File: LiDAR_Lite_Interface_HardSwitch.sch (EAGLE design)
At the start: 30 parts, among them J1 CONN_6SCREW_2.54, J2 CONN_42.54_SCREW, Q1 2N7002, Q2 2N7002, Q3 DMG3404, Q4 MOSFET_PCH-NX2301P, U1 TLV61220DBV, U2 TS5A23157DGS

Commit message: Updated layout, added variants
Improved layout, potentially add button, then ready to send to fab. Added variations of layout for potential future alteration
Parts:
- removed U2: TS5A23157DGS, bschulz:TS5A23157DGS
- added S1: SWITCH_DPDTJS_GULLWING, bschulz:SWITCH_DPDTJS_GULLWING
- C1: DIGIKEY (none) -> 493-2182-1-ND; MF (none) -> Nichicon; MPN (none) -> UWT1C681MNL1GS
- D1: DIGIKEY (none) -> 732-4978-1-ND; MF (none) -> Wurth; MPN (none) -> 150060RS75000
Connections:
- removed net OUTPUT_CTRL: U2.IN1, U2.IN2, U3.PA6
- net 5V: no longer U2.VCC
- net GND: no longer U2.GND
- net POWER_SW: now also U3.PA6; no longer U3.PA5
- net RX: now also S1.O2; no longer U2.NO2
- net SCL: now also S1.S2; no longer U2.NC1
- net SDA: now also S1.S1; no longer U2.NC2
- net SIG1: now also S1.P1; no longer U2.COM1
- net SIG2: now also S1.P2; no longer U2.COM2
- net TX: now also S1.O1; no longer U2.NO1
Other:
- note added: "RED"
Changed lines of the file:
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@@
 <part name="R1" library="bschulz_passives" deviceset="R-EU_" device="R0603" technology="4.7K" value="4.7k"/>
 <part name="R2" library="bschulz_passives" deviceset="R-EU_" device="R0603" technology="4.7K" value="4.7k"/>
-<part name="C1" library="bschulz_passives" deviceset="CPOL-EU" device="UW-10X10"/>
+<part name="C1" library="bschulz_passives" deviceset="CPOL-EU" device="UW-10X10">
+<spice>
+<pinmapping spiceprefix="C">
+<pinmap gate="G$1" pin="+" pinorder="1"/>
+<pinmap gate="G$1" pin="-" pinorder="2"/>
+</pinmapping>
+</spice>
+<attribute name="DIGIKEY" value="493-2182-1-ND"/>
+<attribute name="MF" value="Nichicon"/>
+<attribute name="MPN" value="UWT1C681MNL1GS"/>
+</part>
 <part name="GND1" library="supply1" library_urn="urn:adsk.eagle:library:371" deviceset="GND" device=""/>
 <part name="Q1" library="bschulz" deviceset="MOSFET-NCH" device="-2N7002P" value="2N7002"/>
@@
 <part name="R9" library="bschulz_passives" deviceset="R-EU_" device="R0603" technology="10K" value="10k"/>
 <part name="GND6" library="supply1" library_urn="urn:adsk.eagle:library:371" deviceset="GND" device=""/>
-<part name="D1" library="bschulz" deviceset="LED" device="0603" value="LED0603"/>
+<part name="D1" library="bschulz" deviceset="LED" device="0603" value="LED0603">
+<attribute name="DIGIKEY" value="732-4978-1-ND"/>
+<attribute name="MF" value="Wurth"/>
+<attribute name="MPN" value="150060RS75000"/>
+</part>
 <part name="R10" library="bschulz_passives" deviceset="R-EU_" device="R0603" technology="330"/>
 <part name="GND20" library="supply1" library_urn="urn:adsk.eagle:library:371" deviceset="GND" device=""/>
 <part name="R11" library="bschulz_passives" deviceset="R-EU_" device="R0603" technology="1K" value="1k"/>
-<part name="U2" library="bschulz" deviceset="TS5A23157" device="DGS"/>
+<part name="S1" library="bschulz" deviceset="SWITCH_DPDT" device="JS_GULLWING"/>
 </parts>
 <sheets>
@@
 <plain>
 <text x="-22.86" y="7.62" size="1.778" layer="91">Software I2C!</text>
+<text x="5.08" y="71.12" size="1.778" layer="91" rot="R90">RED</text>
 </plain>
 <instances>
@@
 <attribute name="NAME" x="26.543" y="38.5826" size="1.778" layer="95"/>
 <attribute name="VALUE" x="26.543" y="33.5026" size="1.778" layer="96"/>
+<attribute name="MPN" x="25.4" y="38.1" size="1.778" layer="96" display="off"/>
+<attribute name="MF" x="25.4" y="38.1" size="1.778" layer="96" display="off"/>
+<attribute name="DIGIKEY" x="25.4" y="38.1" size="1.778" layer="96" display="off"/>
 </instance>
 <instance part="GND1" gate="1" x="25.4" y="27.94" smashed="yes">
@@
 <attribute name="VALUE" x="113.03" y="95.758" size="1.778" layer="96"/>
 </instance>
-<instance part="U2" gate="G$1" x="152.4" y="81.28" smashed="yes">
-<attribute name="DISP" x="152.4" y="95.758" size="1.778" layer="95" ratio="15" align="center"/>
-<attribute name="NAME" x="152.4" y="64.008" size="1.778" layer="95" ratio="15" align="center"/>
+<instance part="S1" gate="G$1" x="147.32" y="76.2" smashed="yes" rot="R180">
+<attribute name="VALUE" x="148.59" y="82.55" size="1.778" layer="96" font="vector" rot="R180" align="top-center"/>
+<attribute name="NAME" x="148.59" y="67.818" size="1.778" layer="95" font="vector" rot="R180" align="bottom-center"/>
 </instance>
 </instances>
@@
 <wire x1="10.16" y1="68.58" x2="10.16" y2="66.04" width="0.1524" layer="91"/>
 <pinref part="GND20" gate="1" pin="GND"/>
-</segment>
-<segment>
-<pinref part="U2" gate="G$1" pin="GND"/>
-<wire x1="139.7" y1="88.9" x2="134.62" y2="88.9" width="0.1524" layer="91"/>
-<label x="134.62" y="88.9" size="1.778" layer="95" rot="R180" xref="yes"/>
 </segment>
 <segment>
@@
 </segment>
 <segment>
-<pinref part="U2" gate="G$1" pin="NC2"/>
-<wire x1="139.7" y1="71.12" x2="134.62" y2="71.12" width="0.1524" layer="91"/>
-<label x="134.62" y="71.12" size="1.778" layer="95" rot="R180" xref="yes"/>
+<wire x1="144.78" y1="73.66" x2="139.7" y2="73.66" width="0.1524" layer="91"/>
+<label x="139.7" y="73.66" size="1.778" layer="95" rot="R180" xref="yes"/>
+<pinref part="S1" gate="G$1" pin="S1"/>
 </segment>
 </net>
@@
 </segment>
 <segment>
-<pinref part="U2" gate="G$1" pin="NC1"/>
-<wire x1="139.7" y1="81.28" x2="134.62" y2="81.28" width="0.1524" layer="91"/>
-<label x="134.62" y="81.28" size="1.778" layer="95" rot="R180" xref="yes"/>
+<wire x1="144.78" y1="81.28" x2="139.7" y2="81.28" width="0.1524" layer="91"/>
+<label x="139.7" y="81.28" size="1.778" layer="95" rot="R180" xref="yes"/>
+<pinref part="S1" gate="G$1" pin="S2"/>
 </segment>
 </net>
@@
 </segment>
 <segment>
-<pinref part="U2" gate="G$1" pin="COM2"/>
-<wire x1="165.1" y1="73.66" x2="172.72" y2="73.66" width="0.1524" layer="91"/>
-<label x="172.72" y="73.66" size="1.778" layer="95" xref="yes"/>
+<wire x1="152.4" y1="78.74" x2="160.02" y2="78.74" width="0.1524" layer="91"/>
+<label x="160.02" y="78.74" size="1.778" layer="95" xref="yes"/>
+<pinref part="S1" gate="G$1" pin="P2"/>
 </segment>
 </net>
@@
 </segment>
 <segment>
-<pinref part="U2" gate="G$1" pin="COM1"/>
-<wire x1="165.1" y1="83.82" x2="172.72" y2="83.82" width="0.1524" layer="91"/>
-<label x="172.72" y="83.82" size="1.778" layer="95" xref="yes"/>
+<wire x1="152.4" y1="71.12" x2="160.02" y2="71.12" width="0.1524" layer="91"/>
+<label x="160.02" y="71.12" size="1.778" layer="95" xref="yes"/>
+<pinref part="S1" gate="G$1" pin="P1"/>
 </segment>
 </net>
@@
 <label x="99.06" y="86.36" size="1.778" layer="95" xref="yes"/>
 </segment>
-<segment>
-<pinref part="U2" gate="G$1" pin="VCC"/>
-<wire x1="139.7" y1="91.44" x2="134.62" y2="91.44" width="0.1524" layer="91"/>
-<label x="134.62" y="91.44" size="1.778" layer="95" rot="R180" xref="yes"/>
-</segment>
 </net>
 <net name="N$7" class="0">
@@
 </segment>
 <segment>
-<pinref part="U3" gate="G$1" pin="PA5"/>
-<wire x1="50.8" y1="78.74" x2="45.72" y2="78.74" width="0.1524" layer="91"/>
-<label x="45.72" y="78.74" size="1.778" layer="95" rot="R180" xref="yes"/>
+<pinref part="U3" gate="G$1" pin="PA6"/>
+<wire x1="50.8" y1="76.2" x2="45.72" y2="76.2" width="0.1524" layer="91"/>
+<label x="45.72" y="76.2" size="1.778" layer="95" rot="R180" xref="yes"/>
 </segment>
 </net>
@@
 </segment>
 </net>
-<net name="OUTPUT_CTRL" class="0">
-<segment>
-<pinref part="U2" gate="G$1" pin="IN2"/>
-<wire x1="139.7" y1="73.66" x2="134.62" y2="73.66" width="0.1524" layer="91"/>
-<label x="134.62" y="73.66" size="1.778" layer="95" rot="R180" xref="yes"/>
-</segment>
-<segment>
-<pinref part="U2" gate="G$1" pin="IN1"/>
-<wire x1="139.7" y1="83.82" x2="134.62" y2="83.82" width="0.1524" layer="91"/>
-<label x="134.62" y="83.82" size="1.778" layer="95" rot="R180" xref="yes"/>
-</segment>
-<segment>
-<pinref part="U3" gate="G$1" pin="PA6"/>
-<wire x1="50.8" y1="76.2" x2="45.72" y2="76.2" width="0.1524" layer="91"/>
-<label x="45.72" y="76.2" size="1.778" layer="95" rot="R180" xref="yes"/>
-</segment>
-</net>
 <net name="RX" class="0">
 <segment>
@@
 </segment>
 <segment>
-<pinref part="U2" gate="G$1" pin="NO2"/>
-<wire x1="139.7" y1="68.58" x2="134.62" y2="68.58" width="0.1524" layer="91"/>
-<label x="134.62" y="68.58" size="1.778" layer="95" rot="R180" xref="yes"/>
+<wire x1="144.78" y1="76.2" x2="139.7" y2="76.2" width="0.1524" layer="91"/>
+<label x="139.7" y="76.2" size="1.778" layer="95" rot="R180" xref="yes"/>
+<pinref part="S1" gate="G$1" pin="O2"/>
 </segment>
 </net>
@@
 </segment>
 <segment>
-<pinref part="U2" gate="G$1" pin="NO1"/>
-<wire x1="139.7" y1="78.74" x2="134.62" y2="78.74" width="0.1524" layer="91"/>
-<label x="134.62" y="78.74" size="1.778" layer="95" rot="R180" xref="yes"/>
-</segment>
-</net>
+<wire x1="144.78" y1="68.58" x2="139.7" y2="68.58" width="0.1524" layer="91"/>
+<label x="139.7" y="68.58" size="1.778" layer="95" rot="R180" xref="yes"/>
+<pinref part="S1" gate="G$1" pin="O1"/>
+</segment>
+</net>

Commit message: Added accel and hall effect, sent to fab
Updated layout, added accelerometer, hall effect switch, generated gerbers and sent to fab
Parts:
- added C10, C9: 1uF, bschulz_passives:C-EU1UFC0603
- added C11, C12: 0.1uF, bschulz_passives:C-EU0.1UFC0402
- added C7: 0.1uF, bschulz_passives:C-EU10UFC0805
- added C8: 10uF, bschulz_passives:C-EU0.1UFC0603
- added U2: TCS40DPRSOT23, bschulz:TCS40DPRSOT23
- added U4: LIS3DHLGA, bschulz:LIS3DHLGA
- added U5: MIC53653.3SC70, bschulz:MIC53653.3SC70
- added U6: TXS0102DQM, bschulz:TXS0102DQM
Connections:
- new net 3V3: C10.1, C11.1, C7.1, C8.1, U4.CS, U4.VDD, U4.VDD_IO, U5.VOUT, U6.EN, U6.VA
- new net ACCEL_INT: U3.PA1, U4.INT1
- new net SCL_OB_LV: U4.SCL, U6.A1
- new net SDA_OB_LV: U4.SDA, U6.A2
- new net SWITCH_OUT: U2.OUT, U3.PA0
- net 5V: now also C12.1, C9.1, U2.VCC, U5.EN, U5.VIN, U6.VB
- net GND: now also C10.2, C11.2, C12.2, C7.2, C8.2, C9.2, U2.GND, U4.GND, U4.SA0, U5.GND, U6.GND
- net SCL_OB: now also U6.B1
- net SDA_OB: now also U6.B2
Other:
- note added: "ADD CAP??"

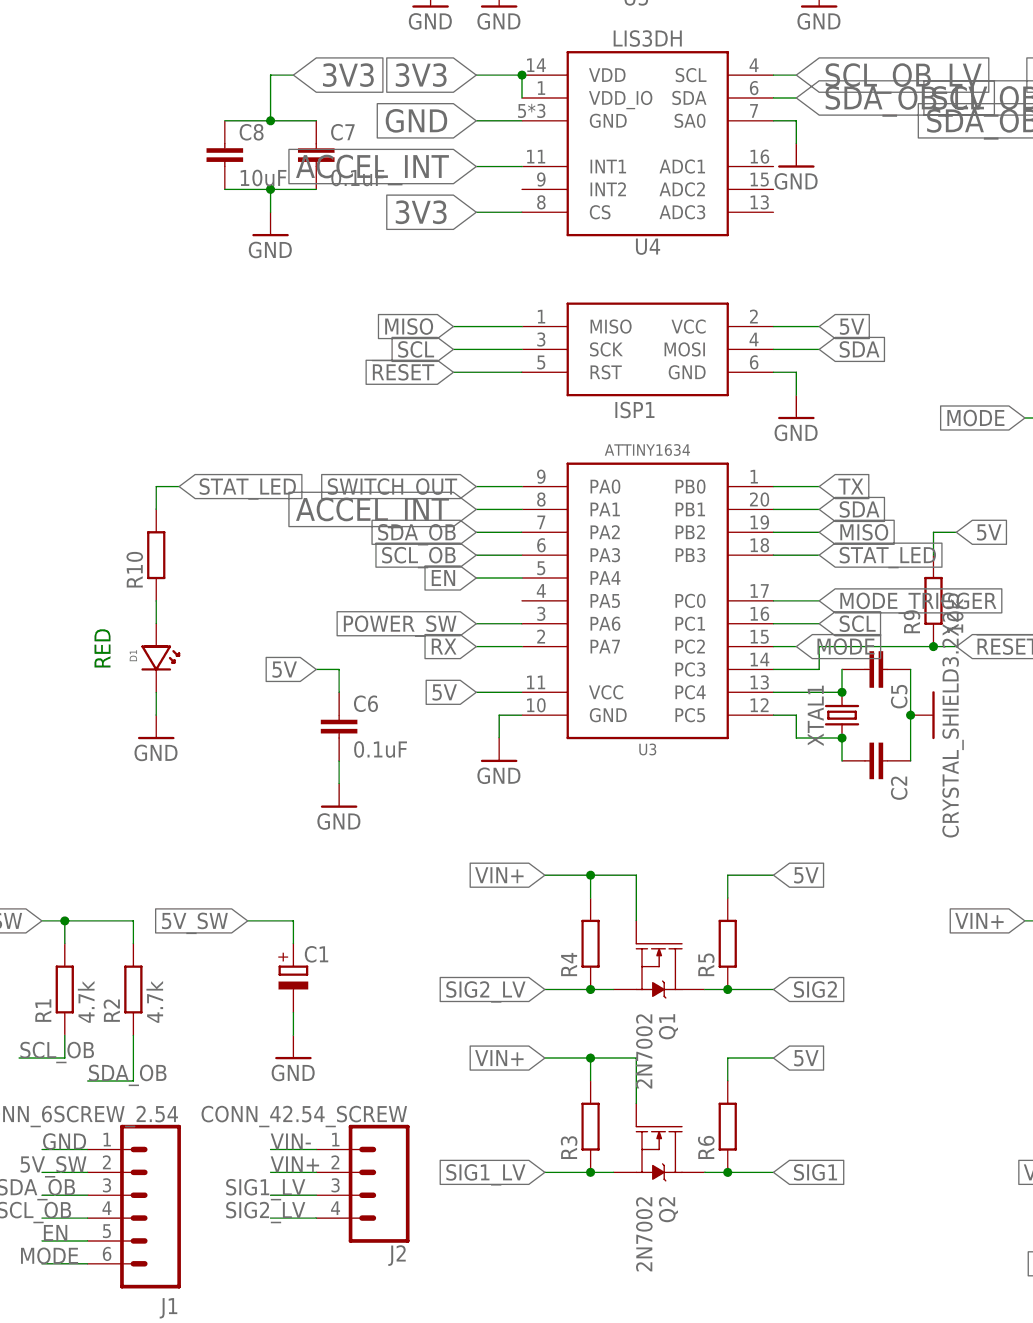
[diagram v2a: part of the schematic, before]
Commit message: Minor value updates, generated BoM
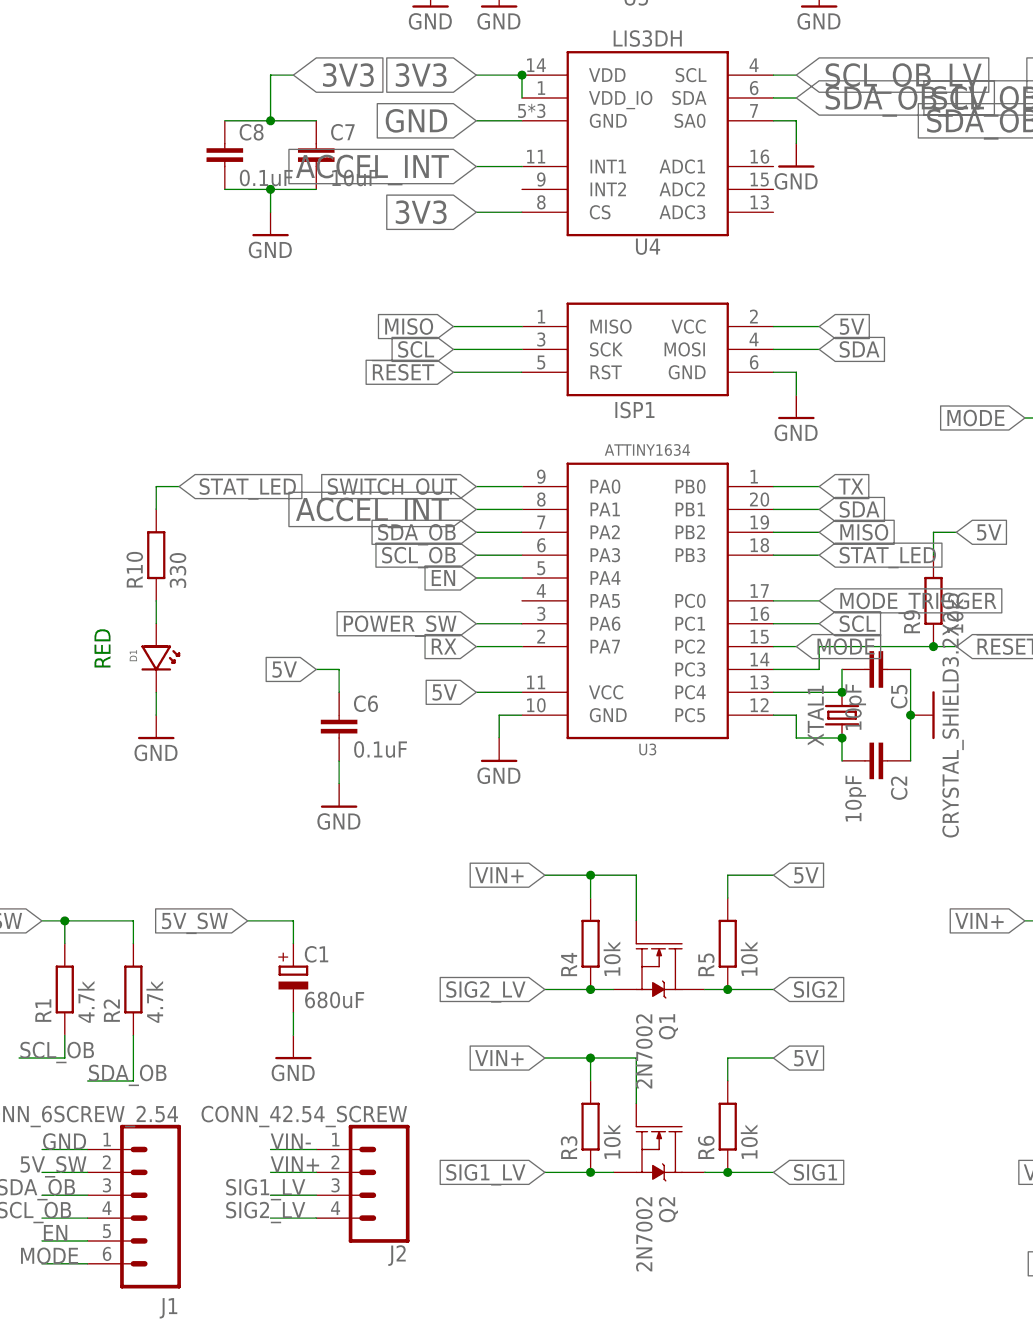
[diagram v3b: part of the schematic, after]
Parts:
- C1: value (none) -> 680uF
- C2, C5: value (none) -> 10pF
- C7: value 0.1uF -> 10uF
- C8: value 10uF -> 0.1uF
- R10: value (none) -> 330
- R3, R4, R5, R6: value (none) -> 10k
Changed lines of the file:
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@@
 <part name="R1" library="bschulz_passives" deviceset="R-EU_" device="R0603" technology="4.7K" value="4.7k"/>
 <part name="R2" library="bschulz_passives" deviceset="R-EU_" device="R0603" technology="4.7K" value="4.7k"/>
-<part name="C1" library="bschulz_passives" deviceset="CPOL-EU" device="UW-10X10">
+<part name="C1" library="bschulz_passives" deviceset="CPOL-EU" device="UW-10X10" value="680uF">
 <spice>
 <pinmapping spiceprefix="C">
@@
 <part name="Q1" library="bschulz" deviceset="MOSFET-NCH" device="-2N7002P" value="2N7002"/>
 <part name="Q2" library="bschulz" deviceset="MOSFET-NCH" device="-2N7002P" value="2N7002"/>
-<part name="R3" library="bschulz_passives" deviceset="R-EU_" device="R0603" technology="10K"/>
-<part name="R4" library="bschulz_passives" deviceset="R-EU_" device="R0603" technology="10K"/>
-<part name="R5" library="bschulz_passives" deviceset="R-EU_" device="R0603" technology="10K"/>
-<part name="R6" library="bschulz_passives" deviceset="R-EU_" device="R0603" technology="10K"/>
+<part name="R3" library="bschulz_passives" deviceset="R-EU_" device="R0603" technology="10K" value="10k"/>
+<part name="R4" library="bschulz_passives" deviceset="R-EU_" device="R0603" technology="10K" value="10k"/>
+<part name="R5" library="bschulz_passives" deviceset="R-EU_" device="R0603" technology="10K" value="10k"/>
+<part name="R6" library="bschulz_passives" deviceset="R-EU_" device="R0603" technology="10K" value="10k"/>
 <part name="Q3" library="bschulz" deviceset="MOSFET-NCH" device="-DMG3404L" value="DMG3404"/>
 <part name="U1" library="bschulz" deviceset="TLV61220" device="DBV"/>
@@
 <attribute name="MPN" value="ABM8G-12.000MHZ-4Y-T3"/>
 </part>
-<part name="C2" library="bschulz_passives" deviceset="C-EU" device="C0603" technology="10PF"/>
-<part name="C5" library="bschulz_passives" deviceset="C-EU" device="C0603" technology="10PF"/>
+<part name="C2" library="bschulz_passives" deviceset="C-EU" device="C0603" technology="10PF" value="10pF"/>
+<part name="C5" library="bschulz_passives" deviceset="C-EU" device="C0603" technology="10PF" value="10pF"/>
 <part name="U3" library="bschulz" deviceset="ATTINY1634" device="SOIC"/>
 <part name="GND2" library="supply1" library_urn="urn:adsk.eagle:library:371" deviceset="GND" device=""/>
@@
 <attribute name="MPN" value="150060RS75000"/>
 </part>
-<part name="R10" library="bschulz_passives" deviceset="R-EU_" device="R0603" technology="330"/>
+<part name="R10" library="bschulz_passives" deviceset="R-EU_" device="R0603" technology="330" value="330"/>
 <part name="GND20" library="supply1" library_urn="urn:adsk.eagle:library:371" deviceset="GND" device=""/>
 <part name="R11" library="bschulz_passives" deviceset="R-EU_" device="R0603" technology="1K" value="1k"/>
@@
 <part name="GND7" library="supply1" library_urn="urn:adsk.eagle:library:371" deviceset="GND" device=""/>
 <part name="U4" library="bschulz" deviceset="LIS3DH" device="LGA"/>
-<part name="C7" library="bschulz_passives" deviceset="C-EU" device="C0805" technology="10UF" value="0.1uF"/>
-<part name="C8" library="bschulz_passives" deviceset="C-EU" device="C0603" technology="0.1UF" value="10uF"/>
+<part name="C7" library="bschulz_passives" deviceset="C-EU" device="C0805" technology="10UF" value="10uF"/>
+<part name="C8" library="bschulz_passives" deviceset="C-EU" device="C0603" technology="0.1UF" value="0.1uF"/>
 <part name="GND9" library="supply1" library_urn="urn:adsk.eagle:library:371" deviceset="GND" device=""/>
 <part name="U5" library="bschulz" deviceset="MIC5365" device="SC70" technology="3.3"/>
